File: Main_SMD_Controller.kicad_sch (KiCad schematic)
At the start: 51 parts, among them J1 2.1-5.5 +12VDC, J10 Vsens, J11 Vin+, J12 Drain, J13 Gate, J14 Source, J2 Switch_Control, J3 +5V, J4 AnalogIO, J5 +12V, J7 VsensJMP, J8 Vin_-, J9 Conn_01x02, P1 Eoshi-chan_Silk, P2 Eoshi-chan_Silk, P3 Eoshi-chan_Silk, P4 Serial_QR, Q1 2N7002K, Q2 TK100E06N1, U1 NJM7805SDL1, U2 4066, U3 AD8226ARZ, U4 S-89713B-K8T2U

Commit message: Signed-off-by: EosinY <theodor338@gmail.com>
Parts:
- removed P3: Eoshi-chan_Silk, Kibishi-chan:Kibishi-chan_17x17mm, symbol Eoshi-chan:Eoshi-chan_Silk
- removed Q2: TK100E06N1, Package_TO_SOT_THT:TO-220-3_Horizontal_TabDown, symbol Device:Q_NMOS_GDS
- C1: value 0.33u -> 0.47u; Akizuki_code (none) -> 114554
- C2, C4, C5, C6: Akizuki_code (none) -> 116143
- C3: Akizuki_code (none) -> 114453
- C7: value 1000p -> 0.01u; footprint Capacitor_SMD:C_0603_1608Metric -> Capacitor_SMD:C_0402_1005Metric; Akizuki_code (none) -> 116112
- C8: footprint Capacitor_SMD:C_0603_1608Metric -> Capacitor_SMD:C_0402_1005Metric; Akizuki_code (none) -> 116112
- D1: Akizuki_code (none) -> 106014
- J1: Akizuki_code (none) -> 106568
- J10: renamed from J8; Akizuki_code (none) -> 112148
- J11: renamed from J9; Akizuki_code (none) -> 112247
- J12: renamed from J10; Akizuki_code (none) -> 112148
- J13: renamed from J11; Akizuki_code (none) -> 112148
- J2: Akizuki_code (none) -> 112250
- J3, J5: Akizuki_code (none) -> 112247
- J4: Akizuki_code (none) -> 112249
- J6: renamed from J7; Akizuki_code (none) -> 103949
- J7: renamed from J12; Akizuki_code (none) -> 112148
- J8: renamed from J13; Akizuki_code (none) -> 112247
- J9: renamed from J14; Akizuki_code (none) -> 112148
- P2: footprint Eoshi-chan_v2:Eoshi-chan-v2_15x15 -> Eoshi-chan_v2:Eoshi-chan-v2_10x10
- P3: renamed from P4; footprint JLCPCB_Serial:Serial_QR_8x8 -> JLCPCB_Serial:Serial_QR_5x5
- Q1: Akizuki_code (none) -> 104256
- R11: renamed from R12; Akizuki_code (none) -> 106668
- R12: renamed from R11; Akizuki_code (none) -> 106668
- RLY1: Akizuki_code (none) -> 117418
- RV1: Akizuki_code (none) -> 112705
- TH1: Akizuki_code (none) -> 105251
- U1: Akizuki_code (none) -> 111237
- U2: value 4066 -> TC74HC4066AF(F); Marutsu_code (none) -> M0001-8473
- U3: Akizuki_code (none) -> 117564
- U4: Akizuki_code (none) -> 114063
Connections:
- net TH_1: now reaches J11.1 (Pin_1), TH1.1
- net TH_2: now reaches J11.2 (Pin_2), TH1.2
- net LOAD_ENABLE-G: now reaches J2.4 (Pin_4), Q1.1 (G), R4.2
- net Vmeas_IN: now reaches J6.2 (Pin_2), R10.2
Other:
- moved on the sheet: H1, H2, H3, H4, J11, P1, P2, P3, TH1

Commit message: add BOM
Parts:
- H1, H2, H3, H4, P1, P2, P3: now left out of the parts list
- U2: footprint Package_DMP:DMP-14_10x5_P1.27mm -> Package_SO:SO-14_5.3x10.2mm_P1.27mm
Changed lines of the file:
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@@
 		(at 35.56 148.59 0)
 		(unit 1)
-		(exclude_from_sim no)
-		(in_bom yes)
+		(exclude_from_sim yes)
+		(in_bom no)
 		(on_board yes)
 		(dnp no)
@@
 			)
 		)
-		(property "Footprint" "Package_DMP:DMP-14_10x5_P1.27mm"
+		(property "Footprint" "Package_SO:SO-14_5.3x10.2mm_P1.27mm"
 			(at 73.025 133.35 0)
 			(effects
@@
 		(at 35.56 121.92 0)
 		(unit 1)
-		(exclude_from_sim no)
-		(in_bom yes)
+		(exclude_from_sim yes)
+		(in_bom no)
 		(on_board yes)
 		(dnp no)
@@
 			)
 		)
-		(property "Footprint" "Package_DMP:DMP-14_10x5_P1.27mm"
+		(property "Footprint" "Package_SO:SO-14_5.3x10.2mm_P1.27mm"
 			(at 193.675 135.255 0)
 			(effects
@@
 		(at 35.56 161.925 0)
 		(unit 1)
-		(exclude_from_sim no)
-		(in_bom yes)
+		(exclude_from_sim yes)
+		(in_bom no)
 		(on_board yes)
 		(dnp no)
@@
 		(at 35.56 116.84 0)
 		(unit 1)
-		(exclude_from_sim no)
-		(in_bom yes)
+		(exclude_from_sim yes)
+		(in_bom no)
 		(on_board yes)
 		(dnp no)
@@
 			)
 		)
-		(property "Footprint" "Package_DMP:DMP-14_10x5_P1.27mm"
+		(property "Footprint" "Package_SO:SO-14_5.3x10.2mm_P1.27mm"
 			(at 142.875 97.79 0)
 			(effects
@@
 		(at 35.56 153.035 0)
 		(unit 1)
-		(exclude_from_sim no)
-		(in_bom yes)
+		(exclude_from_sim yes)
+		(in_bom no)
 		(on_board yes)
 		(dnp no)
@@
 		(at 35.56 157.48 0)
 		(unit 1)
-		(exclude_from_sim no)
-		(in_bom yes)
+		(exclude_from_sim yes)
+		(in_bom no)
 		(on_board yes)
 		(dnp no)
@@
 			)
 		)
-		(property "Footprint" "Package_DMP:DMP-14_10x5_P1.27mm"
+		(property "Footprint" "Package_SO:SO-14_5.3x10.2mm_P1.27mm"
 			(at 239.395 138.43 0)
 			(effects
@@
 			)
 		)
-		(property "Footprint" "Package_DMP:DMP-14_10x5_P1.27mm"
+		(property "Footprint" "Package_SO:SO-14_5.3x10.2mm_P1.27mm"
 			(at 193.675 141.605 0)
 			(effects
@@
 		(at 35.56 129.54 0)
 		(unit 1)
-		(exclude_from_sim no)
-		(in_bom yes)
+		(exclude_from_sim yes)
+		(in_bom no)
 		(on_board yes)
 		(dnp no)

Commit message: changed library
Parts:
- J1: footprint Akizuki_BarrelJack:BarrelJack_Horizontal1 -> AM_Conn_BarrelJack:MJ-179P(H)
- J10, J12, J13, J7, J9: footprint Akizuki_ScrewTerminal:ScrewTerminal_01x01_PCB-20 -> AM_Conn_ScrewTerminal:ScrewTerminal_01x01_PCB-20
- RLY1: footprint Akizuki_Relay:HSINDA-943_12A-1C_5p -> AM_Relay:HSINDA-943_12A-1C_5p
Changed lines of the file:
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@@
 			)
 		)
-		(property "Footprint" "Akizuki_ScrewTerminal:ScrewTerminal_01x01_PCB-20"
+		(property "Footprint" "AM_Conn_ScrewTerminal:ScrewTerminal_01x01_PCB-20"
 			(at 252.73 116.205 0)
 			(effects
@@
 			)
 		)
-		(property "Footprint" "Akizuki_Relay:HSINDA-943_12A-1C_5p"
+		(property "Footprint" "AM_Relay:HSINDA-943_12A-1C_5p"
 			(at 168.275 93.98 0)
 			(effects
@@
 			)
 		)
-		(property "Footprint" "Akizuki_ScrewTerminal:ScrewTerminal_01x01_PCB-20"
+		(property "Footprint" "AM_Conn_ScrewTerminal:ScrewTerminal_01x01_PCB-20"
 			(at 240.665 74.93 0)
 			(effects
@@
 			)
 		)
-		(property "Footprint" "Akizuki_BarrelJack:BarrelJack_Horizontal1"
+		(property "Footprint" "AM_Conn_BarrelJack:MJ-179P(H)"
 			(at 26.67 33.401 0)
 			(effects
@@
 			)
 		)
-		(property "Footprint" "Akizuki_ScrewTerminal:ScrewTerminal_01x01_PCB-20"
+		(property "Footprint" "AM_Conn_ScrewTerminal:ScrewTerminal_01x01_PCB-20"
 			(at 240.665 92.71 0)
 			(effects
@@
 			)
 		)
-		(property "Footprint" "Akizuki_ScrewTerminal:ScrewTerminal_01x01_PCB-20"
+		(property "Footprint" "AM_Conn_ScrewTerminal:ScrewTerminal_01x01_PCB-20"
 			(at 263.525 29.845 0)
 			(effects
@@
 			)
 		)
-		(property "Footprint" "Akizuki_ScrewTerminal:ScrewTerminal_01x01_PCB-20"
+		(property "Footprint" "AM_Conn_ScrewTerminal:ScrewTerminal_01x01_PCB-20"
 			(at 263.525 55.88 0)
 			(effects

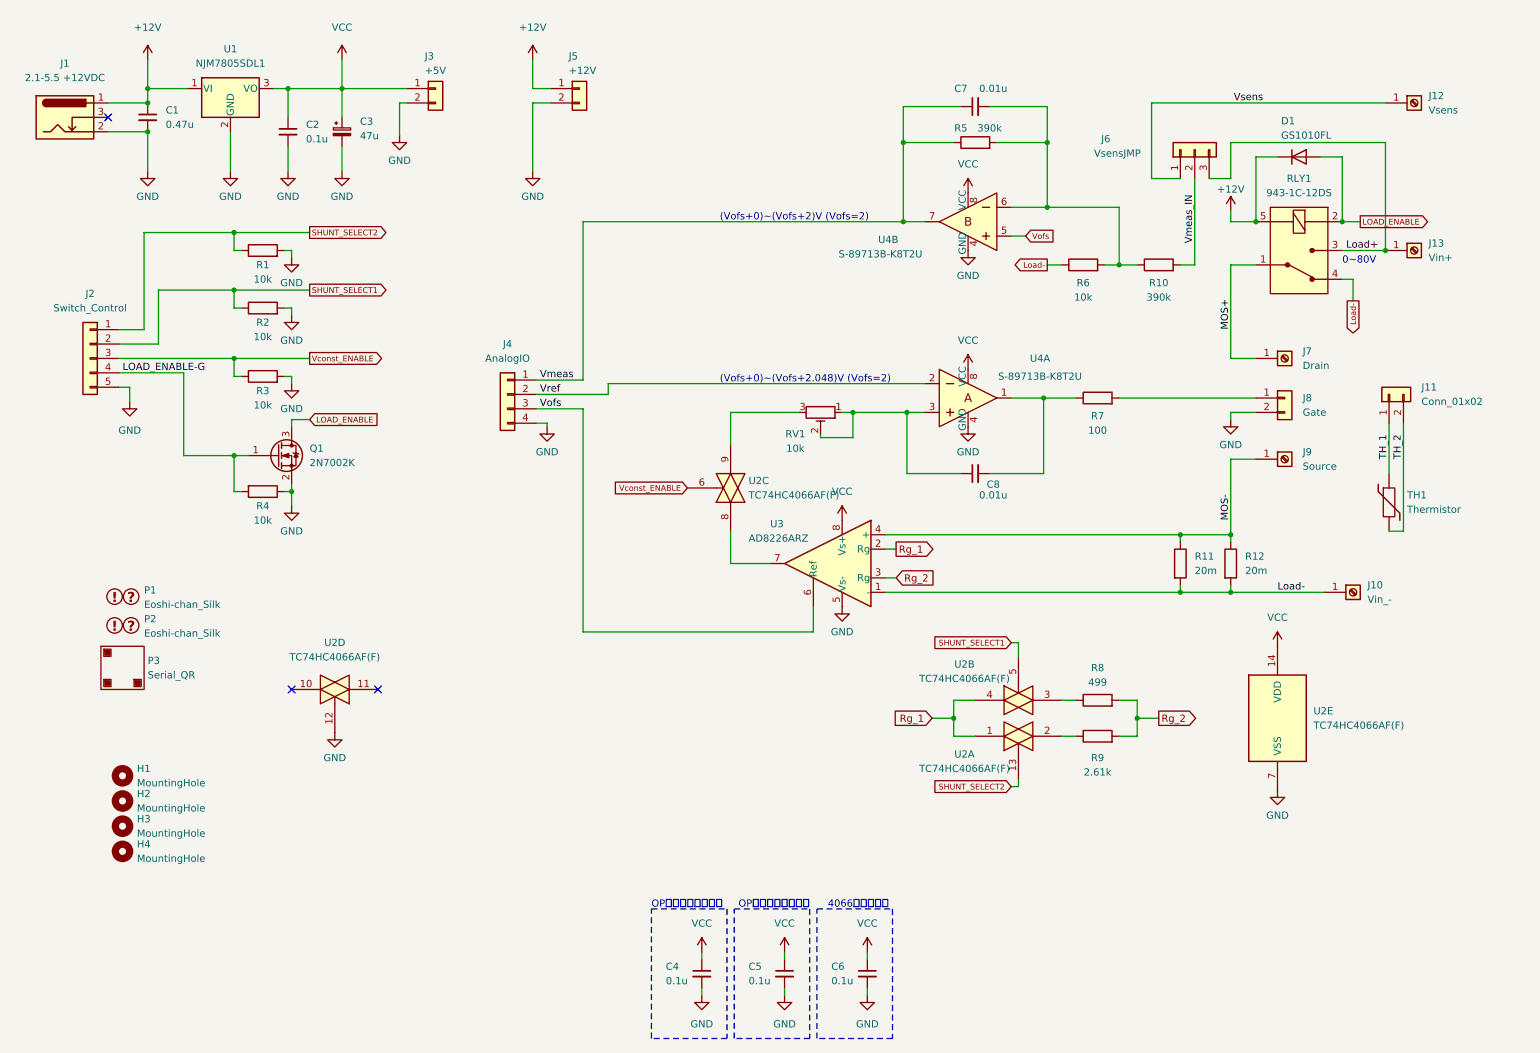
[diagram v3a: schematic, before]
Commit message: Add negative power
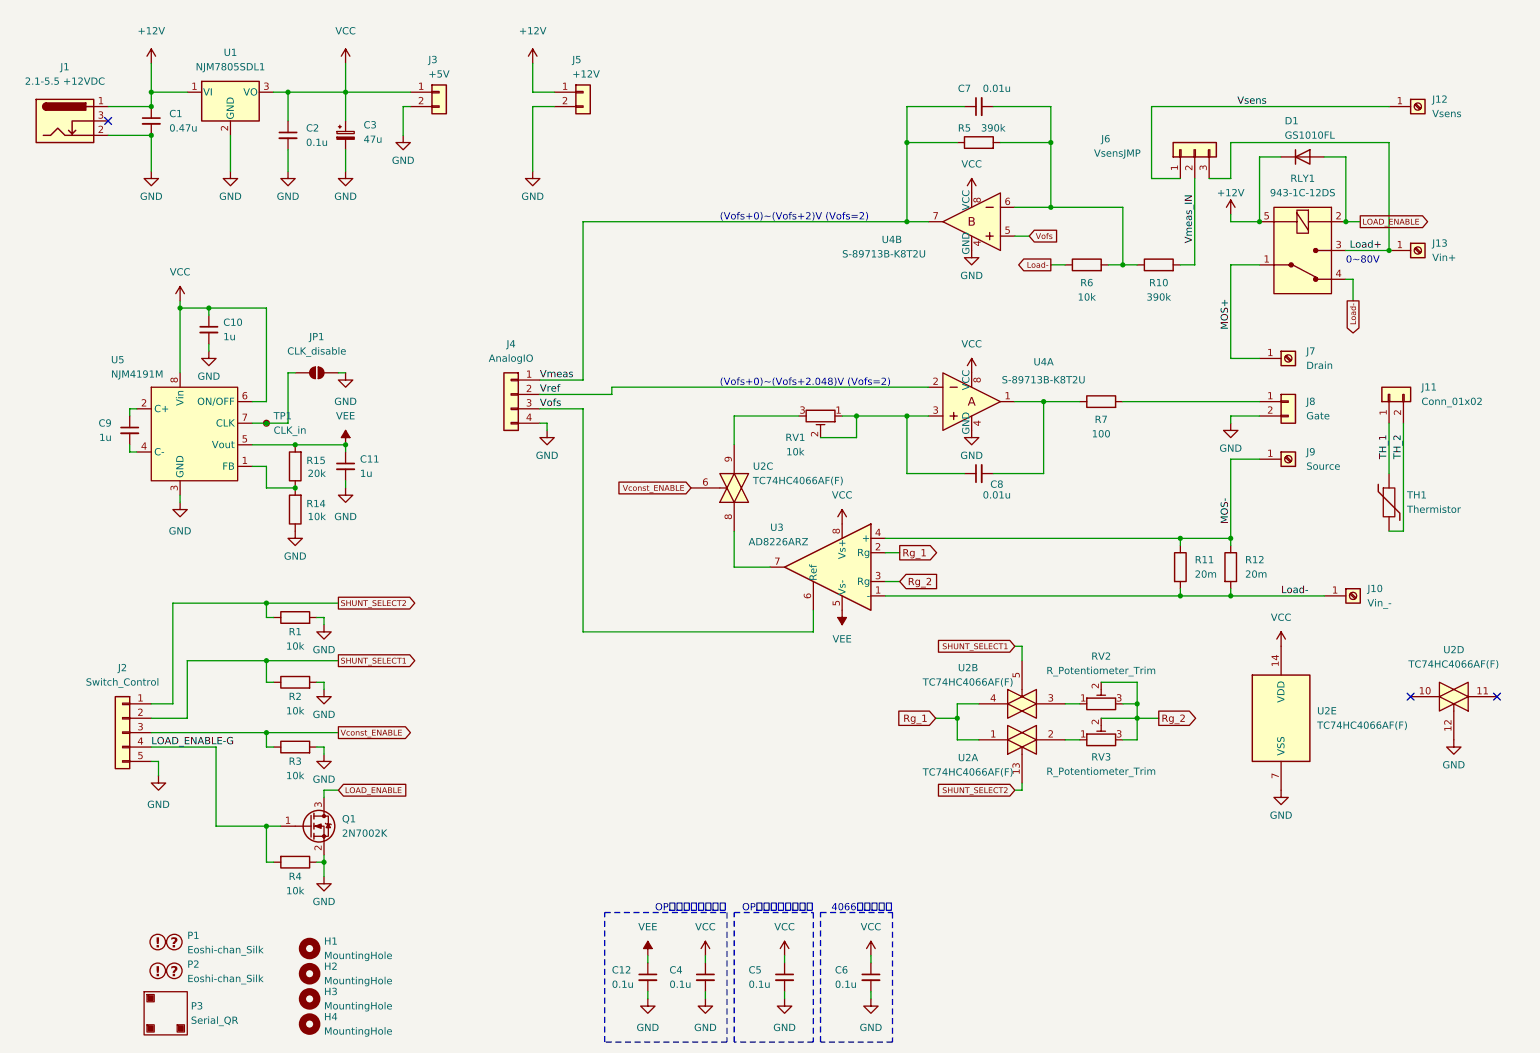
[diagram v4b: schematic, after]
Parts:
- removed R8: 499, Resistor_SMD:R_0603_1608Metric, symbol Device:R
- removed R9: 2.61k, Resistor_SMD:R_0603_1608Metric, symbol Device:R
- added C10, C11, C9: 1u, Capacitor_SMD:C_0603_1608Metric, symbol Device:C_Small
- added C12: 0.1u, Capacitor_SMD:C_0603_1608Metric, symbol Device:C_Small
- added JP1: CLK_disable, Jumper:SolderJumper-2_P1.3mm_Open_TrianglePad1.0x1.5mm, symbol Jumper:SolderJumper_2_Open
- added R14: 10k, Resistor_SMD:R_0603_1608Metric, symbol Device:R
- added R15: 20k, Resistor_SMD:R_0603_1608Metric, symbol Device:R
- added RV2, RV3: R_Potentiometer_Trim, symbol Device:R_Potentiometer_Trim
- added TP1: CLK_in, TestPoint:TestPoint_Pad_2.0x2.0mm, symbol Connector:TestPoint_Small
- added U5: NJM4191M, Package_DMP:DMP-8_5x5_P1.27mm, symbol AM_PowerIC_Switching:NJM4191M
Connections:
- net GND: now also C10.2, C11.2, C12.2, JP1.2 (B), R14.1, U5.3 (GND); no longer U3.5 (Vs-)
- net Rg_2: now also RV2.2, RV2.3, RV3.2, RV3.3
- net VCC: now also C10.1, U5.6 (ON/OFF), U5.8 (Vin)
- net at U2.3: now also RV2.1
- net at U2.2: now also RV3.1
- new net: R14.2, R15.1, U5.1 (FB)
- new net: JP1.1 (A), TP1.1, U5.7 (CLK)
- new net: C9.1, U5.2 (C+)
- new net: C9.2, U5.4 (C-)
- new net VEE: C11.1, C12.1, R15.2, U3.5 (Vs-), U5.5 (Vout)
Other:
- moved on the sheet: C1, C2, C3, C4, C5, C6, C7, C8, D1, H1, H2, H3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

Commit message: alpha 2
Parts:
- R10: footprint Package_DIPSMD:DIPSMD_0W25Resistor_P10.16mm_Horizontal -> Resistor_THT:R_Axial_DIN0207_L6.3mm_D2.5mm_P10.16mm_Horizontal
- R7: renamed from R5; footprint Resistor_SMD:R_0603_1608Metric -> Resistor_THT:R_Axial_DIN0207_L6.3mm_D2.5mm_P5.08mm_Vertical
- R8: renamed from R6; footprint Resistor_SMD:R_0603_1608Metric -> Resistor_THT:R_Axial_DIN0207_L6.3mm_D2.5mm_P10.16mm_Horizontal
- RV1: footprint Potentiometer_SMD:Potentiometer_Bourns_TC33X_Vertical -> AM_Potentiometer:TSR065103R
- RV2, RV3: footprint (none) -> Potentiometer_THT:Potentiometer_Bourns_3296W_Vertical
- U1: renamed from U5; value NJM4191M -> NJW4191M; Akizuki_code (none) -> 114329
- U3: renamed from U2; value TC74HC4066AF(F) -> TC74HC4066AP; footprint Package_SO:SO-14_5.3x10.2mm_P1.27mm -> Package_DIP:DIP-14_W7.62mm_Socket; Akizuki_code (none) -> 105673; Marutsu_code M0001-8473 -> (none)
- renumbered C9 to C1, C6 to C10, C7 to C11, C8 to C12, C1 to C2, C10 to C3, C2 to C4, C3 to C5, C11 to C6, C12 to C7, C4 to C8, C5 to C9, R15 to R1, R14 to R2, R1 to R3, R2 to R4, R3 to R5, R4 to R6, R7 to R9, U1 to U2, U3 to U4, U4 to U5

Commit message: fix pi controller
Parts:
- added D2: D_Schottky, Diode_SMD:D_SOD-323, symbol Device:D_Schottky
- RV2: value R_Potentiometer_Trim -> 500
- RV3: value R_Potentiometer_Trim -> 1k
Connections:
- net +12V: now also D2.1 (K)
- net VCC: now also D2.2 (A)
- net Vref: now also U5.3; no longer U5.2
- net at C12.1, RV1.1, RV1.2: now also U5.2; no longer U5.3
- net Load- renamed R-
- net MOS- renamed R+
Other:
- note added: "0~48V"
- note removed: "0~80V"
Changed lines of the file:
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@@
 		)
 	)
-	(text "0~80V"
+	(text "0~48V"
 		(exclude_from_sim no)
 		(at 251.46 58.42 0)
@@
 	(text "(Vofs+0)~(Vofs+2)V (Vofs=2)"
 		(exclude_from_sim no)
-		(at 140.97 50.8 0)
+		(at 127.254 50.8 0)
 		(effects
 			(font
@@
 	)
 	(junction
+		(at 45.72 27.94)
+		(diameter 0)
+		(color 0 0 0 0)
+	)
+	(junction
 		(at 214.63 138.43)
 		(diameter 0)
@@
 	(wire
 		(pts
+			(xy 45.72 16.51) (xy 45.72 27.94)
+		)
+		(stroke
+			(width 0)
+			(type default)
+		)
+	)
+	(wire
+		(pts
 			(xy 71.12 132.08) (xy 71.12 133.35)
 		)
@@
 	(wire
 		(pts
-			(xy 40.64 27.94) (xy 46.99 27.94)
+			(xy 40.64 27.94) (xy 45.72 27.94)
 		)
 		(stroke
@@
 	(wire
 		(pts
+			(xy 58.42 16.51) (xy 64.77 16.51)
+		)
+		(stroke
+			(width 0)
+			(type default)
+		)
+	)
+	(wire
+		(pts
 			(xy 152.4 180.34) (xy 152.4 181.61)
 		)
@@
 	(wire
 		(pts
+			(xy 64.77 16.51) (xy 64.77 27.94)
+		)
+		(stroke
+			(width 0)
+			(type default)
+		)
+	)
+	(wire
+		(pts
 			(xy 173.99 95.25) (xy 184.15 95.25)
 		)
@@
 	(wire
 		(pts
+			(xy 50.8 16.51) (xy 45.72 16.51)
+		)
+		(stroke
+			(width 0)
+			(type default)
+		)
+	)
+	(wire
+		(pts
 			(xy 121.92 80.01) (xy 177.8 80.01)
 		)
@@
 	(wire
 		(pts
+			(xy 45.72 27.94) (xy 46.99 27.94)
+		)
+		(stroke
+			(width 0)
+			(type default)
+		)
+	)
+	(wire
+		(pts
 			(xy 143.51 85.09) (xy 154.94 85.09)
 		)
@@
 		)
 	)
-	(label "Load-"
-		(at 240.03 116.84 0)
+	(label "R-"
+		(at 234.95 116.84 0)
 		(effects
 			(font
@@
 		)
 	)
-	(label "MOS-"
+	(label "R+"
 		(at 231.14 104.14 90)
 		(effects
@@
 		)
 	)
-	(global_label "Load-"
+	(global_label "R-"
 		(shape output)
 		(at 199.39 58.42 180)
@@
 		)
 		(property "Intersheetrefs" "${INTERSHEET_REFS}"
-			(at 192.6215 58.3565 0)
+			(at 194.7282 58.42 0)
 			(effects
 				(font
@@
 		)
 	)
-	(global_label "Load-"
+	(global_label "R-"
 		(shape output)
 		(at 252.73 64.77 270)
@@
 		)
 		(property "Intersheetrefs" "${INTERSHEET_REFS}"
-			(at 252.6665 71.5385 90)
+			(at 252.73 69.4318 90)
 			(effects
 				(font
@@
 			)
 		)
-		(property "Value" "R_Potentiometer_Trim"
+		(property "Value" "1k"
 			(at 208.28 147.828 90)
 			(effects
@@
 	)
 	(symbol
+		(lib_name "LM358N_Obsolete_1")
 		(lib_id "dk_Linear-Amplifiers-Instrumentation-OP-Amps-Buffer-Amps:LM358N_Obsolete")
 		(at 185.42 50.8 0)
@@
 		(dnp no)
 		(property "Reference" "U5"
-			(at 169.545 53.975 0)
+			(at 172.72 43.815 0)
 			(effects
 				(font
 					(size 1.27 1.27)
 				)
-				(justify right)
 			)
 		)
 		(property "Value" "S-89713B-K8T2U"
-			(at 162.56 56.515 0)
+			(at 172.72 46.99 0)
 			(effects
 				(font
 					(size 1.27 1.27)
 				)
-				(justify right)
 			)
 		)
@@
 			)
 		)
-		(property "Value" "R_Potentiometer_Trim"
+		(property "Value" "500"
 			(at 208.28 130.048 90)
 			(effects
@@
 		(lib_id "dk_Linear-Amplifiers-Instrumentation-OP-Amps-Buffer-Amps:LM358N_Obsolete")
 		(at 185.42 82.55 0)
+		(mirror x)
 		(unit 1)
 		(exclude_from_sim no)
@@
 		(dnp no)
 		(property "Reference" "U5"
-			(at 198.12 75.565 0)
+			(at 196.596 79.121 0)
 			(effects
 				(font
@@
 		)
 		(property "Value" "S-89713B-K8T2U"
-			(at 198.12 78.74 0)
+			(at 196.596 75.946 0)
 			(effects
 				(font
@@
 		)
 		(property "Footprint" "Package_SO:MSOP-8_3x3mm_P0.65mm"
-			(at 190.5 77.47 0)
+			(at 190.5 87.63 0)
 			(effects
 				(font
@@
 		)
 		(property "Datasheet" "https://akizukidenshi.com/goodsaffix/S89713_J.pdf"
-			(at 190.5 74.93 0)
+			(at 190.5 90.17 0)
 			(effects
 				(font
@@
 		)
 		(property "Description" "IC OPAMP GP 2 CIRCUIT 8DIP"
-			(at 190.5 57.15 0)
+			(at 190.5 107.95 0)
 			(effects
 				(font
@@
 		)
 		(property "Digi-Key_PN" "LM358NFS-ND"
-			(at 190.5 72.39 0)
+			(at 190.5 92.71 0)
 			(effects
 				(font
@@
 		)
 		(property "MPN" "LM358N"
-			(at 190.5 69.85 0)
+			(at 190.5 95.25 0)
 			(effects
 				(font
@@
 		)
 		(property "Category" "Integrated Circuits (ICs)"
-			(at 190.5 67.31 0)
+			(at 190.5 97.79 0)
 			(effects
 				(font
@@
 		)
 		(property "Family" "Linear - Amplifiers - Instrumentation, OP Amps, Buffer Amps"
-			(at 190.5 64.77 0)
+			(at 190.5 100.33 0)
 			(effects
 				(font
@@
 		)
 		(property "DK_Datasheet_Link" "https://www.onsemi.com/pub/Collateral/LM358A-D.pdf"
-			(at 190.5 62.23 0)
+			(at 190.5 102.87 0)
 			(effects
 				(font
@@
 		)
 		(property "DK_Detail_Page" "/product-detail/en/on-semiconductor/LM358N/LM358NFS-ND/458692"
-			(at 190.5 59.69 0)
+			(at 190.5 105.41 0)
 			(effects
 				(font
@@
 		)
 		(property "Manufacturer" "ON Semiconductor"
-			(at 190.5 54.61 0)
+			(at 190.5 110.49 0)
 			(effects
 				(font
@@
 		)
 		(property "Status" "Obsolete NonStock"
-			(at 190.5 52.07 0)
+			(at 190.5 113.03 0)
 			(effects
 				(font
@@
 					(unit 1)
 				)
+			)
+		)
+	)
+	(symbol
+		(lib_id "Device:D_Schottky")
+		(at 54.61 16.51 0)
+		(unit 1)
+		(exclude_from_sim no)
+		(in_bom yes)
+		(on_board yes)
+		(dnp no)
+		(property "Reference" "D2"
+			(at 58.42 14.986 0)
+			(effects
+				(font
+					(size 1.27 1.27)
+				)
+			)
+		)
+		(property "Value" "D_Schottky"
+			(at 66.802 14.986 0)
+			(effects
+				(font
+					(size 1.27 1.27)
+				)
+			)
+		)
+		(property "Footprint" "Diode_SMD:D_SOD-323"
+			(at 54.61 16.51 0)
+			(effects
+				(font
+					(size 1.27 1.27)
+				)
+				(hide yes)
+			)
+		)
+		(property "Datasheet" "~"
+			(at 54.61 16.51 0)
+			(effects
+				(font
+					(size 1.27 1.27)
+				)
+				(hide yes)
+			)
+		)
+		(property "Description" "Schottky diode"
+			(at 54.61 16.51 0)
+			(effects
+				(font
+					(size 1.27 1.27)
+				)
+				(hide yes)
+			)
+		)
+		(pin "1"
+		)
+		(pin "2"
+		)
+		(instances
+			(project ""
+				(path "/cc05fe4a-2c8d-4e81-9d9c-75aa28727c69"
+					(reference "D2")
+					(unit 1)
+				)
